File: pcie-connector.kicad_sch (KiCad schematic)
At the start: 6 parts, among them J10 PCB-Edge_PCIexpress_x8, SW1 CVS-03B

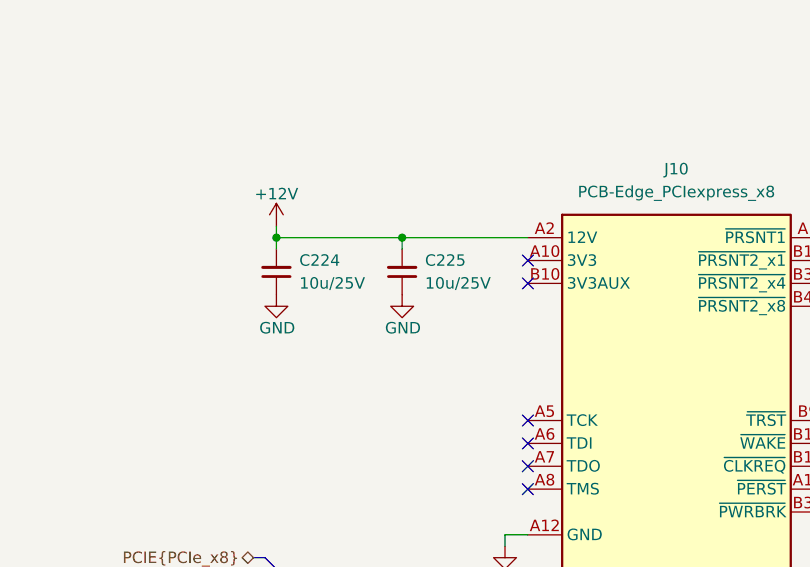
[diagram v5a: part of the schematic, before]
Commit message: [#68016] Solve ERC warrings and errors
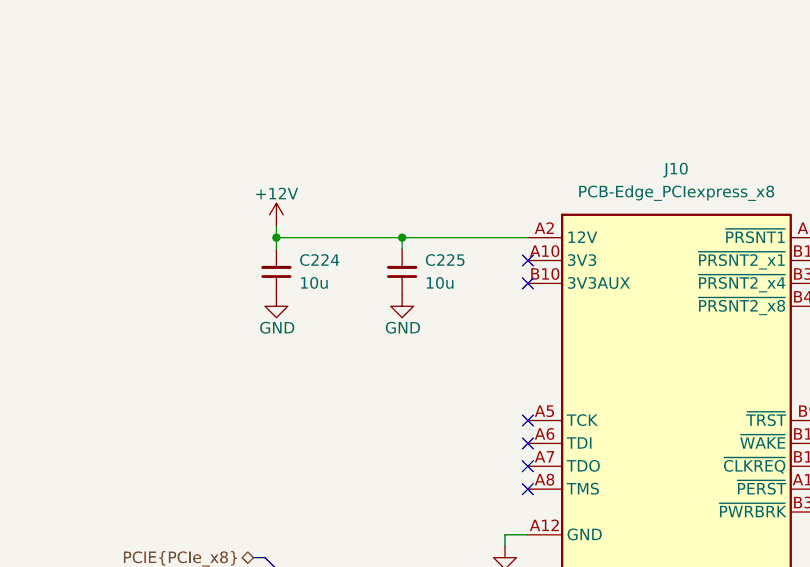
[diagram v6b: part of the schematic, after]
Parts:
- C224, C225: Val 10u/25V -> 10u; Voltage (none) -> 25V
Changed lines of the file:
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@@
       (effects (font (size 1.27 1.27) (thickness 0.15)) (justify left bottom) hide)
     )
-    (property "Val" "10u/25V" (at 181.61 73.6535 90)
+    (property "Val" "10u" (at 181.61 73.6535 90)
       (effects (font (size 1.27 1.27) (thickness 0.15)) (justify right))
     )
-    (property "Voltage" "" (at 207.01 54.61 0)
+    (property "Voltage" "25V" (at 207.01 54.61 0)
       (effects (font (size 1.27 1.27)) (justify left bottom) hide)
     )
@@
       (effects (font (size 1.27 1.27) (thickness 0.15)) (justify left bottom) hide)
     )
-    (property "Val" "10u/25V" (at 167.64 73.6535 90)
+    (property "Val" "10u" (at 167.64 73.6535 90)
       (effects (font (size 1.27 1.27) (thickness 0.15)) (justify right))
     )
-    (property "Voltage" "" (at 193.04 54.61 0)
+    (property "Voltage" "25V" (at 193.04 54.61 0)
       (effects (font (size 1.27 1.27)) (justify left bottom) hide)
     )
